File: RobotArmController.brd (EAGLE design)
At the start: 85.3 x 34.8 mm, 67 parts, among them M1 M02LOCK, M1C3 0.1uf, M1C4 0.1uf, M2 M02LOCK, M2C3 0.1uf, M2C4 0.1uf, M3 M02LOCK, M3C3 0.1uf, M3C4 0.1uf, M4 M02LOCK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

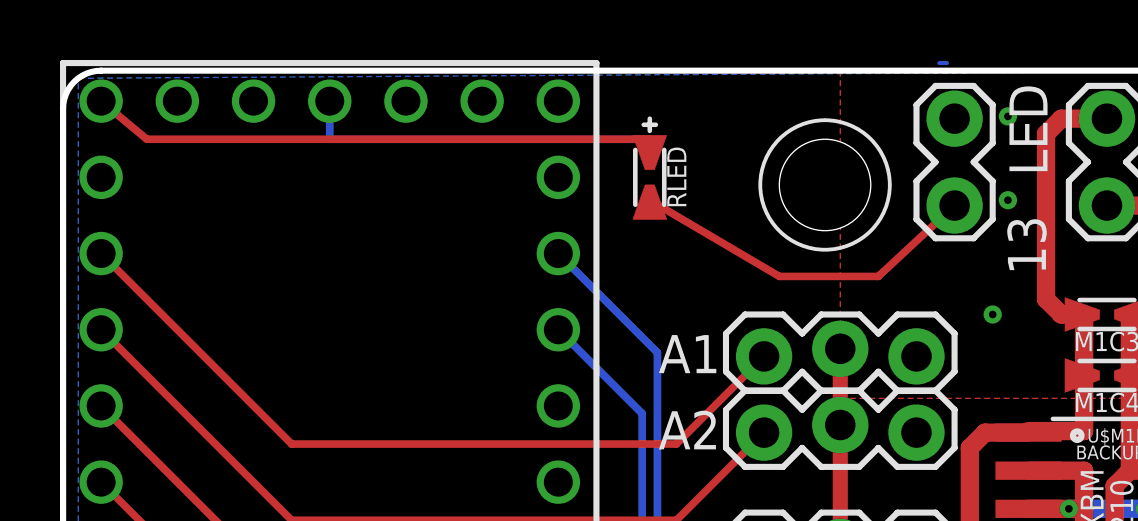
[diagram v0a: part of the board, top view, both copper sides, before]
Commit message: Remove LED resistor (not used)
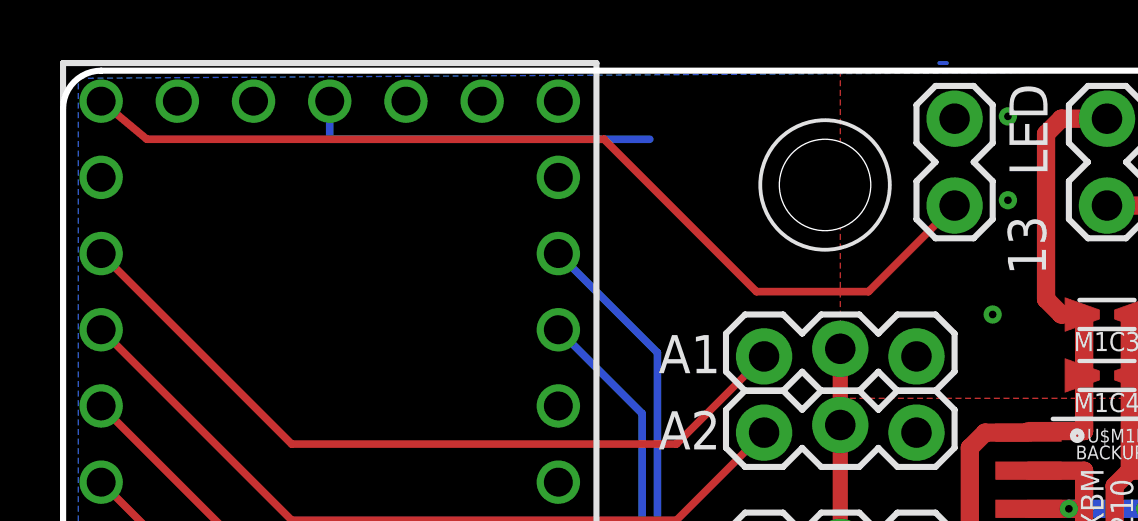
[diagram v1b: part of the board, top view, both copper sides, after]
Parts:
- removed RLED: (no value), tekdemo:0402-0603-0805-UNIVERSAL
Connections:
- removed net N$1: LED.2, RLED.-
- net T13/LED: now also LED.2; no longer RLED.+
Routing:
- net T13/LED: track 19.3 -> 32.2 mm
- net N$1: track 11.8 -> 0.00 mm
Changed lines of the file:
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@@
 <grid distance="10" unitdist="mil" unit="mil" style="lines" multiple="5" display="yes" altdistance="1" altunitdist="mil" altunit="mil"/>
 <layers>
-<layer number="1" name="Top" color="4" fill="11" visible="no" active="yes"/>
-<layer number="16" name="Bottom" color="1" fill="11" visible="no" active="yes"/>
+<layer number="1" name="Top" color="4" fill="11" visible="yes" active="yes"/>
+<layer number="16" name="Bottom" color="1" fill="11" visible="yes" active="yes"/>
 <layer number="17" name="Pads" color="2" fill="1" visible="yes" active="yes"/>
 <layer number="18" name="Vias" color="2" fill="1" visible="yes" active="yes"/>
@@
 <layer number="45" name="Holes" color="7" fill="1" visible="yes" active="yes"/>
 <layer number="46" name="Milling" color="3" fill="1" visible="no" active="yes"/>
-<layer number="47" name="Measures" color="7" fill="1" visible="yes" active="yes"/>
+<layer number="47" name="Measures" color="7" fill="1" visible="no" active="yes"/>
 <layer number="48" name="Document" color="7" fill="1" visible="no" active="yes"/>
 <layer number="49" name="Reference" color="7" fill="1" visible="no" active="yes"/>
@@
 <element name="U$11" library="tekdemo" package="NET-JUNCTION-2" value="NET-JUNCTION-2" x="78.994" y="17.526" rot="R270"/>
 <element name="U$13" library="tekdemo" package="NET-JUNCTION-2" value="NET-JUNCTION-2" x="27.94" y="45.212" rot="MR180"/>
-<element name="RLED" library="tekdemo" package="0402-0603-0805-UNIVERSAL" value="" x="18.288" y="41.402" rot="R270"/>
 <element name="LED" library="tekdemo" package="1X02_LOCK" value="M02LOCK" x="28.448" y="43.18" smashed="yes" rot="R270">
 <attribute name="NAME" x="30.2768" y="44.5262" size="1.27" layer="25" ratio="15" rot="R270"/>
@@
 <signal name="T13/LED" class="1">
 <contactref element="TEENSY" pad="13"/>
-<contactref element="RLED" pad="+"/>
 <wire x1="0" y1="43.942" x2="1.524" y2="42.672" width="0.254" layer="1"/>
-<wire x1="1.524" y1="42.672" x2="18.288" y2="42.672" width="0.254" layer="1"/>
-<wire x1="18.288" y1="42.672" x2="18.288" y2="42.164" width="0.254" layer="1"/>
+<wire x1="1.524" y1="42.672" x2="16.764" y2="42.672" width="0.254" layer="1"/>
+<contactref element="LED" pad="2"/>
+<wire x1="16.764" y1="42.672" x2="21.844" y2="37.592" width="0.254" layer="1"/>
+<wire x1="21.844" y1="37.592" x2="25.5778" y2="37.592" width="0.254" layer="1"/>
+<wire x1="25.5778" y1="37.592" x2="28.448" y2="40.4622" width="0.254" layer="1"/>
 </signal>
 <signal name="T6/PWM" class="1">
@@
 <wire x1="17.78" y1="20.828" x2="17.526" y2="21.082" width="0.254" layer="16"/>
 </signal>
-<signal name="N$1" class="1">
-<contactref element="LED" pad="2"/>
-<contactref element="RLED" pad="-"/>
-<wire x1="18.288" y1="40.64" x2="22.606" y2="38.1" width="0.254" layer="1"/>
-<wire x1="22.606" y1="38.1" x2="25.908" y2="38.1" width="0.254" layer="1"/>
-<wire x1="25.908" y1="38.1" x2="28.448" y2="40.4622" width="0.254" layer="1"/>
-</signal>
 </signals>

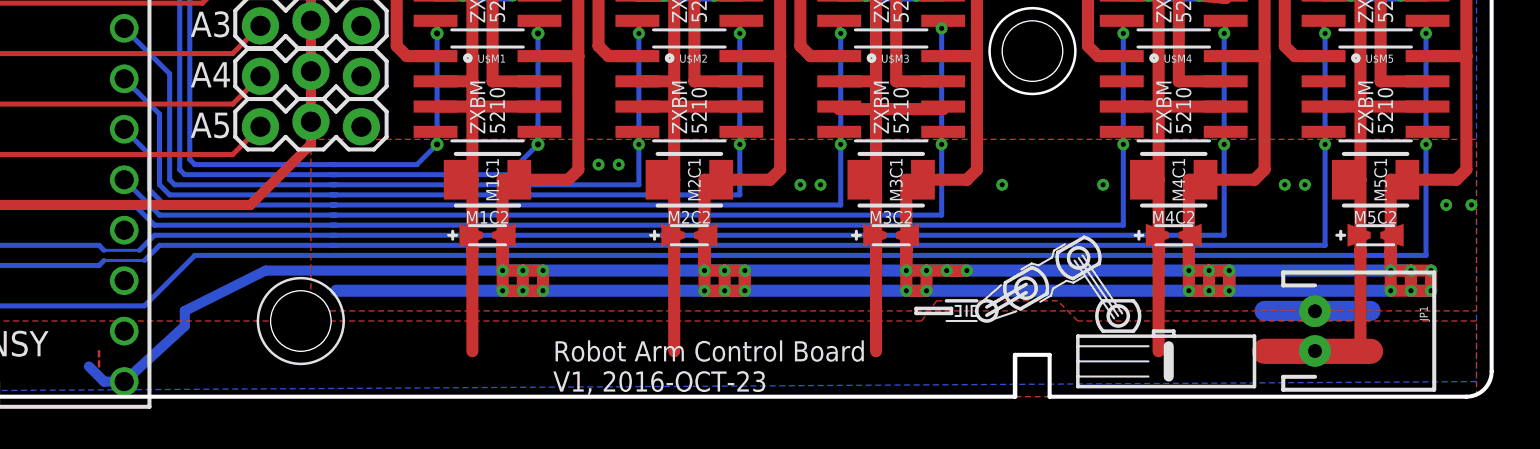
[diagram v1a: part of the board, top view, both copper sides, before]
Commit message: Add OWI power connector, update gnd plane, silk
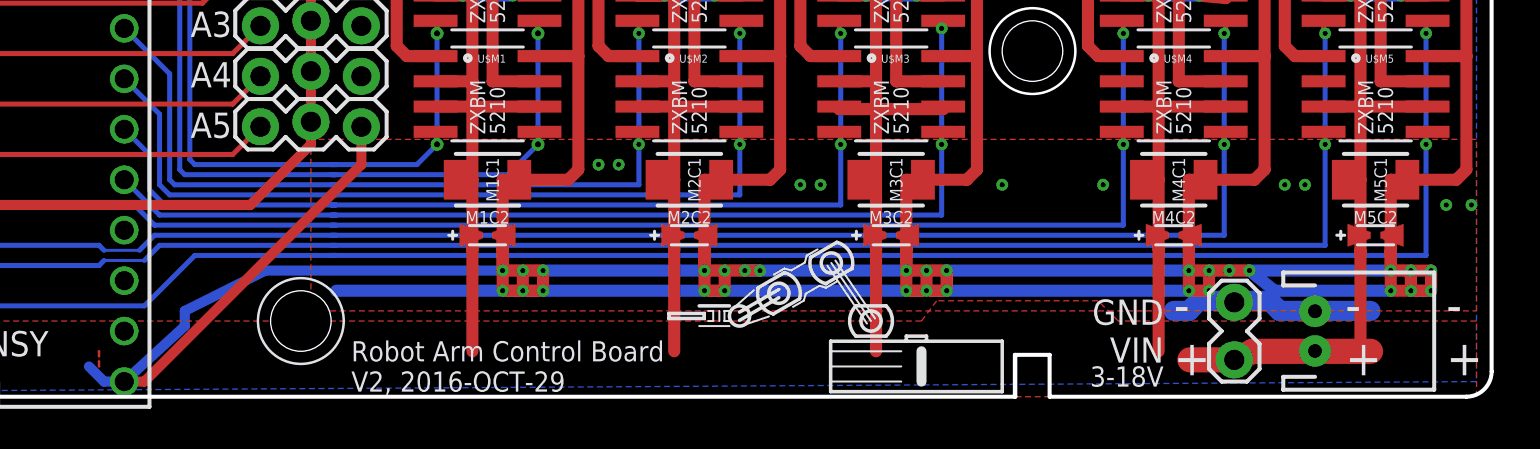
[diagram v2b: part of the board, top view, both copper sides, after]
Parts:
- added JP2: M02LOCK, tekdemo:1X02_LOCK
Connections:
- net GND: now also JP2.1
- net VIN: now also JP2.2
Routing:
- net GND: track 196.3 -> 215.6 mm
- net VIN: track 31.7 -> 35.6 mm
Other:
- board text added: "- +"
- board text added: "3-18V"
- board text added: "GND VIN"
- board text added: "Robot Arm Control Board V2, 2016-OCT-29"
- board text removed: "Robot Arm Control Board V1, 2016-OCT-23"

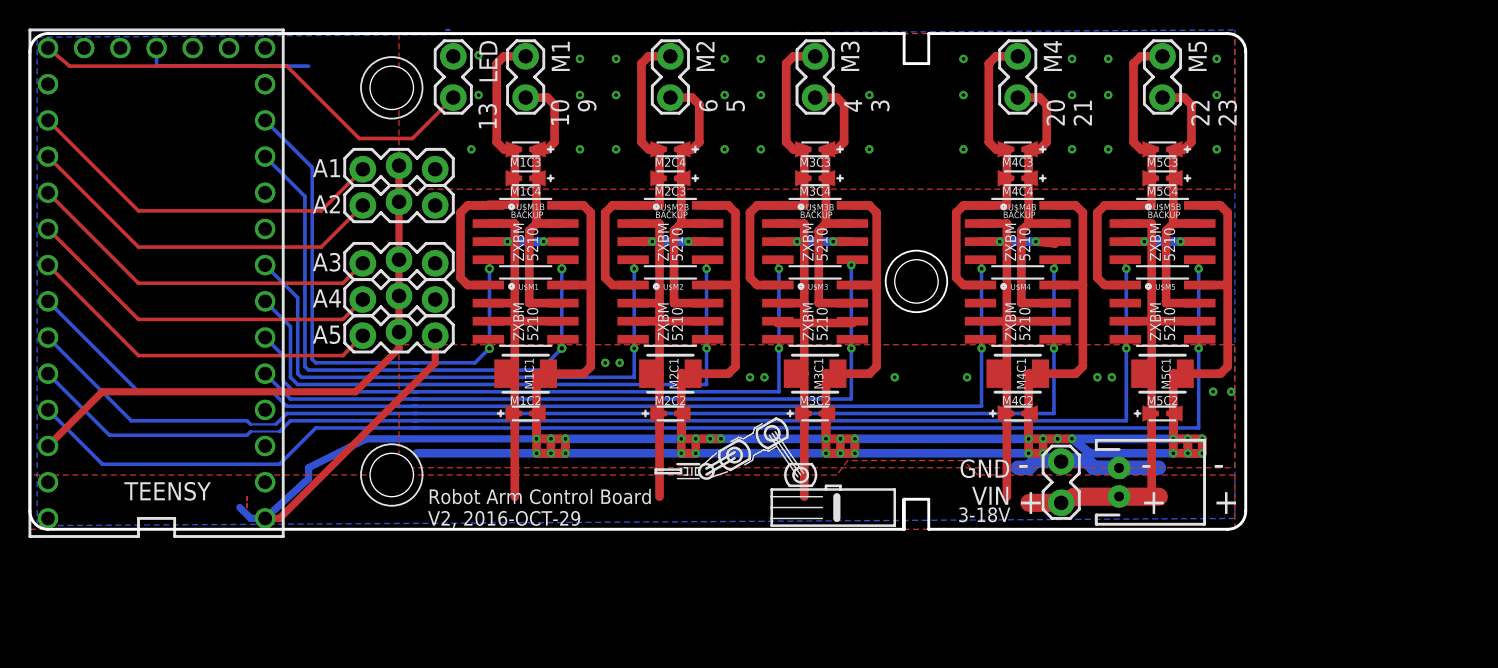
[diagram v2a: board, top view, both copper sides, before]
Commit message: Add controller input
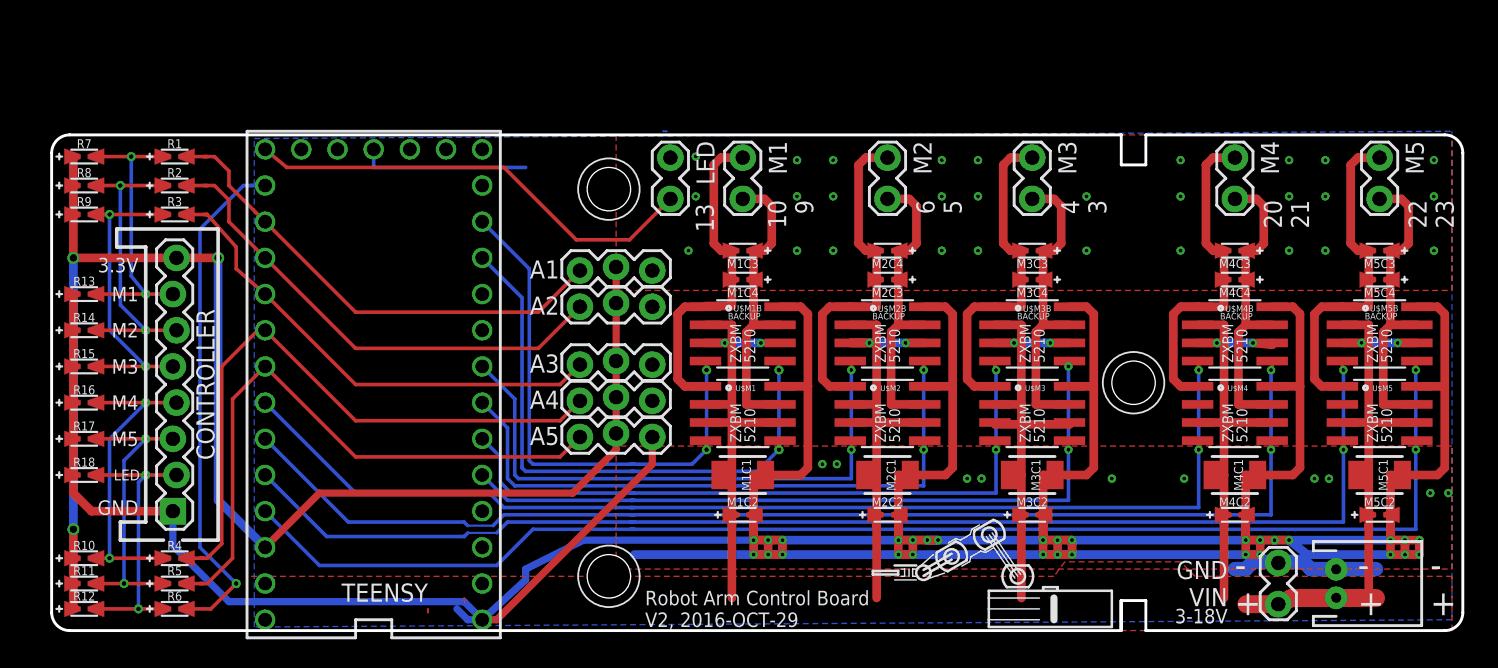
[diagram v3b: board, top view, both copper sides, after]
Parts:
- added CONTROLLER: (no value), SparkFun-Connectors:1X08_LOCK
- added R1, R10, R11, R12, R13, R14, R15, R16, R17, R18, R2, R3, R4, R5, R6, R7, R8, R9: 1k, tekdemo:0402-0603-0805-UNIVERSAL
- added U$12, U$25, U$26, U$27, U$28, U$29: NET-JUNCTION-2, tekdemo:NET-JUNCTION-2
- moved JP1 16.8 mm to (90.4, 6.35)
- moved LED 16.8 mm to (43.7, 36.1)
- moved M1 16.8 mm to (48.8, 36.1)
- moved M1C4 16.8 mm to (48.8, 27.7)
- moved U$1 16.8 mm to (48.0, 10.7)
- moved U$14 16.8 mm to (41.1, 14.7)
- moved U$18 16.8 mm to (41.1, 12.7)
- moved U$2 16.8 mm to (49.5, 10.7)
- moved U$22 16.8 mm to (41.1, 10.7)
- moved U$4 16.8 mm to (29.2, 5.33)
- moved A1 16.8 mm to (42.4, 28.4)
- moved A2 16.8 mm to (42.4, 25.9)
- moved A4 16.8 mm to (42.4, 19.3)
- moved A5 16.8 mm to (42.4, 16.8)
- moved M1C1 16.8 mm to (48.8, 14.0)
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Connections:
- new net J1: CONTROLLER.7, R1.+, R13.-, R7.-
- new net J2: CONTROLLER.6, R14.-, R2.+, R8.-
- new net J3: CONTROLLER.5, R15.-, R3.+, R9.-
- new net J4: CONTROLLER.4, R10.-, R16.-, R4.+
- new net J5: CONTROLLER.3, R11.-, R17.-, R5.+
- new net JL: CONTROLLER.2, R12.-, R18.-, R6.+
- new net JLED: R6.-, U$29.P$1
- new net JM1: R1.-, U$12.P$1
- new net JM2: R2.-, U$25.P$1
- new net JM3: R3.-, U$26.P$1
- new net JM4: R4.-, U$27.P$1
- new net JM5: R5.-, U$28.P$1
- net 3.3V: now also CONTROLLER.8, R10.+, R11.+, R12.+, R7.+, R8.+, R9.+
- net GND: now also CONTROLLER.1, R13.+, R14.+, R15.+, R16.+, R17.+, R18.+
- net T14/A0: now also U$29.P$2
- net T15/A1: now also U$12.P$2
- net T16/A2: now also U$25.P$2
- net T17/A3: now also U$26.P$2
- net T18/A4: now also U$27.P$2
- net T19/A5: now also U$28.P$2
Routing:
- net 3.3V: track 40.3 -> 103.9 mm, vias 0 -> 3
- net GND: track 215.6 -> 263.4 mm
- net JLED: track 0.00 -> 35.3 mm, vias 0 -> 1
- net J4: track 0.00 -> 22.5 mm, vias 0 -> 2
- net J3: track 0.00 -> 22.0 mm, vias 0 -> 2
- net J2: track 0.00 -> 21.4 mm, vias 0 -> 2
- net J5: track 0.00 -> 21.1 mm, vias 0 -> 2
- net J1: track 0.00 -> 20.3 mm, vias 0 -> 2
- net JL: track 0.00 -> 20.1 mm, vias 0 -> 2
- net T18/A4: track 25.3 -> 43.8 mm
- net T19/A5: track 25.3 -> 42.7 mm
- net T17/A3: track 25.3 -> 32.8 mm
- net T16/A2: track 25.9 -> 33.3 mm
- net T15/A1: track 25.9 -> 32.7 mm
- net JM3: track 0.00 -> 1.52 mm
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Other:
- board size 85.3 x 34.8 mm -> 99.1 x 34.8 mm
- board text added: "3.3V"
- board text added: "GND"
- board text added: "LED"
- board text added: "M1"
- board text added: "M2"
- board text added: "M3"
- board text added: "M4"
- board text added: "M5"
